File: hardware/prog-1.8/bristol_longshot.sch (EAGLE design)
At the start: 5 parts, among them IC3 TLV70018DCK

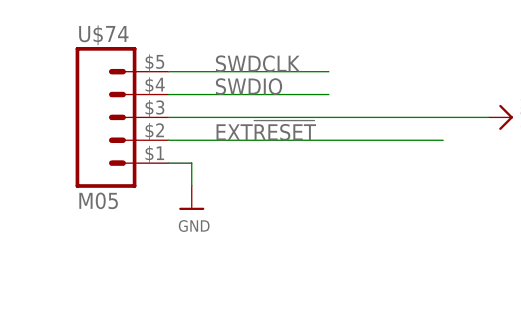
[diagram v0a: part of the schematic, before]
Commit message: Updated many parts lists, updated bard numbering, removed makefiles for inactive things
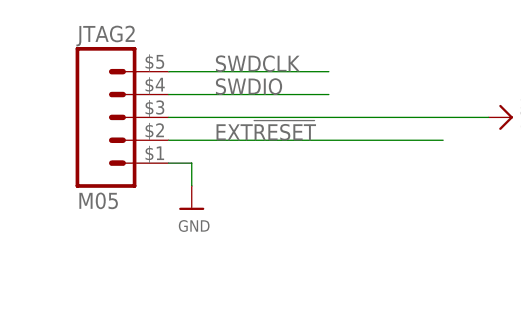
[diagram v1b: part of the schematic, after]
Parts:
- renumbered IC3 to U1, U$74 to JTAG2
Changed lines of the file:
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@@
 <part name="FRAME1" library="SparkFun" deviceset="FRAME-LETTER" device=""/>
 <part name="U$6" library="microbuilder_v3" deviceset="GND" device=""/>
-<part name="U$74" library="fbri" deviceset="M05" device=""/>
+<part name="JTAG2" library="fbri" deviceset="M05" device=""/>
 <part name="U$1" library="microbuilder_v3" deviceset="GND" device=""/>
 <part name="JTAG1" library="microbuilder_v3" deviceset="JTAG-CORTEXM3" device="SMT"/>
 <part name="U$2" library="microbuilder_v3" deviceset="3.3V" device=""/>
 <part name="U$34" library="microbuilder_v3" deviceset="1.8V" device=""/>
-<part name="IC3" library="tlv700" deviceset="TLV700" device="DCK" value="TLV70018DCK"/>
+<part name="U1" library="tlv700" deviceset="TLV700" device="DCK" value="TLV70018DCK"/>
 <part name="U$70" library="microbuilder" deviceset="GND" device=""/>
 <part name="U$83" library="microbuilder" deviceset="GND" device=""/>
@@
 <instance part="FRAME1" gate="G$2" x="147.32" y="0"/>
 <instance part="U$6" gate="G$1" x="30.48" y="152.4"/>
-<instance part="U$74" gate="A" x="22.86" y="162.56"/>
+<instance part="JTAG2" gate="A" x="22.86" y="162.56"/>
 <instance part="U$1" gate="G$1" x="12.7" y="106.68"/>
 <instance part="JTAG1" gate="G$1" x="25.4" y="114.3"/>
 <instance part="U$2" gate="G$1" x="12.7" y="137.16"/>
 <instance part="U$34" gate="G$1" x="162.56" y="160.02" rot="MR0"/>
-<instance part="IC3" gate="G$1" x="137.16" y="142.24"/>
+<instance part="U1" gate="G$1" x="137.16" y="142.24"/>
 <instance part="U$70" gate="G$1" x="144.78" y="132.08"/>
 <instance part="U$83" gate="G$1" x="124.46" y="132.08"/>
@@
 <net name="GND" class="0">
 <segment>
-<pinref part="U$74" gate="A" pin="1"/>
+<pinref part="JTAG2" gate="A" pin="1"/>
 <wire x1="27.94" y1="157.48" x2="30.48" y2="157.48" width="0.1524" layer="91"/>
 <pinref part="U$6" gate="G$1" pin="GND"/>
@@
 <segment>
 <pinref part="U$70" gate="G$1" pin="GND"/>
-<pinref part="IC3" gate="G$1" pin="GND"/>
+<pinref part="U1" gate="G$1" pin="GND"/>
 <wire x1="144.78" y1="134.62" x2="144.78" y2="137.16" width="0.1524" layer="91"/>
 </segment>
@@
 <net name="SWDIO" class="0">
 <segment>
-<pinref part="U$74" gate="A" pin="4"/>
+<pinref part="JTAG2" gate="A" pin="4"/>
 <wire x1="27.94" y1="165.1" x2="45.72" y2="165.1" width="0.1524" layer="91"/>
 <label x="33.02" y="165.1" size="1.778" layer="95"/>
@@
 <net name="SWDCLK" class="0">
 <segment>
-<pinref part="U$74" gate="A" pin="5"/>
+<pinref part="JTAG2" gate="A" pin="5"/>
 <wire x1="27.94" y1="167.64" x2="45.72" y2="167.64" width="0.1524" layer="91"/>
 <label x="33.02" y="167.64" size="1.778" layer="95"/>
@@
 <net name="EXT!RESET" class="0">
 <segment>
-<pinref part="U$74" gate="A" pin="2"/>
+<pinref part="JTAG2" gate="A" pin="2"/>
 <wire x1="27.94" y1="160.02" x2="58.42" y2="160.02" width="0.1524" layer="91"/>
 <label x="33.02" y="160.02" size="1.778" layer="95"/>
@@
 <segment>
 <wire x1="124.46" y1="152.4" x2="124.46" y2="147.32" width="0.1524" layer="91"/>
-<pinref part="IC3" gate="G$1" pin="IN"/>
+<pinref part="U1" gate="G$1" pin="IN"/>
 <wire x1="124.46" y1="147.32" x2="124.46" y2="144.78" width="0.1524" layer="91"/>
 <wire x1="132.08" y1="147.32" x2="129.54" y2="147.32" width="0.1524" layer="91"/>
 <junction x="124.46" y="147.32"/>
-<pinref part="IC3" gate="G$1" pin="EN"/>
+<pinref part="U1" gate="G$1" pin="EN"/>
 <wire x1="129.54" y1="147.32" x2="124.46" y2="147.32" width="0.1524" layer="91"/>
 <wire x1="129.54" y1="144.78" x2="132.08" y2="144.78" width="0.1524" layer="91"/>
@@
 <net name="1.8V" class="0">
 <segment>
-<pinref part="IC3" gate="G$1" pin="OUT"/>
+<pinref part="U1" gate="G$1" pin="OUT"/>
 <wire x1="157.48" y1="147.32" x2="162.56" y2="147.32" width="0.1524" layer="91"/>
 <wire x1="162.56" y1="147.32" x2="162.56" y2="144.78" width="0.1524" layer="91"/>
@@
 </segment>
 <segment>
-<pinref part="U$74" gate="A" pin="3"/>
+<pinref part="JTAG2" gate="A" pin="3"/>
 <wire x1="27.94" y1="162.56" x2="63.5" y2="162.56" width="0.1524" layer="91"/>
 <pinref part="U$3" gate="G$1" pin="1.8V"/>
